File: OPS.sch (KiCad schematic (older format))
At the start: 92 parts, among them J1 USB, J2 PWR, J3 Banana, J4 Banana, J5 CON_PWR, J6 CON_DATA, J7 M3, P1 TC2030, Q1 SS8050, Q2 AO3400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

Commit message: routing 60%
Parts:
- C10, C15: value 100n -> 22u; footprint otter:C_0402 -> otter:C_0805
- C16, C20, C9: value 10u -> 22u
- C17, C8: footprint Capacitor_Tantalum_SMD:CP_EIA-7343-31_Kemet-D -> Capacitor_SMD:CP_Elec_6.3x5.8
- J6: footprint Connector_PinHeader_2.00mm:PinHeader_1x07_P2.00mm_Vertical -> Connector_PinHeader_2.00mm:PinHeader_1x08_P2.00mm_Vertical; symbol Connector_Generic:Conn_01x07 -> Connector_Generic:Conn_01x08
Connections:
- net +3V3: now also J6.4 (Pin_4)
- net INT_MP_1: now also J6.6 (Pin_6); no longer J6.5 (Pin_5)
- net LED_GREEN: now also U3.39 (PB3); no longer U3.40 (PB4)
- net LED_RED: now also U3.40 (PB4); no longer U3.39 (PB3)
- net OUT_EN_1: now also J6.5 (Pin_5); no longer J6.4 (Pin_4)
- net SCL: now also J6.7 (Pin_7); no longer J6.6 (Pin_6)
- net SDA: now also J6.8 (Pin_8); no longer J6.7 (Pin_7)
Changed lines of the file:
@@
 	7050 6300 7050 6400
 Connection ~ 7050 6300
-$Comp
-L Device:C_Small C10
-U 1 1 60808E89
-P 6700 6500
-F 0 "C10" H 6792 6546 50  0000 L CNN
-F 1 "100n" H 6792 6455 50  0000 L CNN
-F 2 "otter:C_0402" H 6700 6500 50  0001 C CNN
-F 3 "~" H 6700 6500 50  0001 C CNN
-	1    6700 6500
-	1    0    0    -1
-$EndComp
 Wire Wire Line
 	6700 6300 6700 6400
@@
 	6050 6250 6050 6300
 $Comp
-L otter:GND #PWR0137
-U 1 1 6082C1E8
-P 6700 6600
-F 0 "#PWR0137" H 6700 6350 50  0001 C CNN
-F 1 "GND" H 6705 6427 50  0000 C CNN
-F 2 "" H 6700 6600 60  0000 C CNN
-F 3 "" H 6700 6600 60  0000 C CNN
-	1    6700 6600
-	1    0    0    -1
-$EndComp
-$Comp
 L Device:C_Small C9
 U 1 1 60831902
 P 6400 6500
 F 0 "C9" H 6492 6546 50  0000 L CNN
-F 1 "10u" H 6492 6455 50  0000 L CNN
+F 1 "22u" H 6492 6455 50  0000 L CNN
 F 2 "otter:C_0805" H 6400 6500 50  0001 C CNN
 F 3 "~" H 6400 6500 50  0001 C CNN
@@
 F 0 "C8" H 6168 6496 50  0000 L CNN
 F 1 "47u" H 6168 6405 50  0000 L CNN
-F 2 "Capacitor_Tantalum_SMD:CP_EIA-7343-31_Kemet-D" H 6088 6300 50  0001 C CNN
+F 2 "Capacitor_SMD:CP_Elec_6.3x5.8" H 6088 6300 50  0001 C CNN
 F 3 "~" H 6050 6450 50  0001 C CNN
 	1    6050 6450
@@
 $EndComp
 $Comp
-L Device:C_Small C15
-U 1 1 6084818D
-P 8850 6900
-F 0 "C15" H 8942 6946 50  0000 L CNN
-F 1 "100n" H 8942 6855 50  0000 L CNN
-F 2 "otter:C_0402" H 8850 6900 50  0001 C CNN
-F 3 "~" H 8850 6900 50  0001 C CNN
-	1    8850 6900
-	1    0    0    -1
-$EndComp
-$Comp
-L otter:GND #PWR0140
-U 1 1 60848193
-P 8850 7000
-F 0 "#PWR0140" H 8850 6750 50  0001 C CNN
-F 1 "GND" H 8855 6827 50  0000 C CNN
-F 2 "" H 8850 7000 60  0000 C CNN
-F 3 "" H 8850 7000 60  0000 C CNN
-	1    8850 7000
-	1    0    0    -1
-$EndComp
-$Comp
 L Device:C_Small C16
 U 1 1 6084AEE7
 P 9200 6900
 F 0 "C16" H 9292 6946 50  0000 L CNN
-F 1 "10u" H 9292 6855 50  0000 L CNN
+F 1 "22u" H 9292 6855 50  0000 L CNN
 F 2 "otter:C_0805" H 9200 6900 50  0001 C CNN
 F 3 "~" H 9200 6900 50  0001 C CNN
@@
 F 0 "C17" H 9668 6946 50  0000 L CNN
 F 1 "47u" H 9668 6855 50  0000 L CNN
-F 2 "Capacitor_Tantalum_SMD:CP_EIA-7343-31_Kemet-D" H 9588 6750 50  0001 C CNN
+F 2 "Capacitor_SMD:CP_Elec_6.3x5.8" H 9588 6750 50  0001 C CNN
 F 3 "~" H 9550 6900 50  0001 C CNN
 	1    9550 6900
@@
 P 11800 6900
 F 0 "C20" H 11892 6946 50  0000 L CNN
-F 1 "10u" H 11892 6855 50  0000 L CNN
+F 1 "22u" H 11892 6855 50  0000 L CNN
 F 2 "otter:C_0805" H 11800 6900 50  0001 C CNN
 F 3 "~" H 11800 6900 50  0001 C CNN
@@
 Text GLabel 14250 7050 2    50   Input ~ 0
 LED_RED
+Text GLabel 8400 2800 0    50   Input ~ 0
+LED_GREEN
 Text GLabel 8400 2900 0    50   Input ~ 0
-LED_GREEN
-Text GLabel 8400 2800 0    50   Input ~ 0
 LED_RED
 Text Notes 13950 7350 0    50   ~ 0
@@
 	8050 3200 7800 3200
 Connection ~ 7800 3200
-Text GLabel 5650 5050 0    50   Input ~ 0
+Text GLabel 5650 5150 0    50   Input ~ 0
 INT_MP_1
-Text GLabel 5650 5150 0    50   Input ~ 0
+Text GLabel 5650 5250 0    50   Input ~ 0
 SCL
-Text GLabel 5650 5250 0    50   Input ~ 0
+Text GLabel 5650 5350 0    50   Input ~ 0
 SDA
 $Comp
-L Connector_Generic:Conn_01x07 J6
+L Connector_Generic:Conn_01x08 J6
 U 1 1 60960B7E
 P 5850 4950
 F 0 "J6" H 5930 4992 50  0000 L CNN
 F 1 "CON_DATA" H 5930 4901 50  0000 L CNN
-F 2 "Connector_PinHeader_2.00mm:PinHeader_1x07_P2.00mm_Vertical" H 5850 4950 50  0001 C CNN
+F 2 "Connector_PinHeader_2.00mm:PinHeader_1x08_P2.00mm_Vertical" H 5850 4950 50  0001 C CNN
 F 3 "~" H 5850 4950 50  0001 C CNN
 	1    5850 4950
@@
 Text GLabel 11350 3400 2    50   Input ~ 0
 OUT_EN_1
-Text GLabel 5650 4950 0    50   Input ~ 0
+Text GLabel 5650 5050 0    50   Input ~ 0
 OUT_EN_1
 $Comp
@@
 Wire Wire Line
 	10200 3200 9700 3200
+$Comp
+L Device:C_Small C10
+U 1 1 60860E99
+P 6700 6500
+F 0 "C10" H 6792 6546 50  0000 L CNN
+F 1 "22u" H 6792 6455 50  0000 L CNN
+F 2 "otter:C_0805" H 6700 6500 50  0001 C CNN
+F 3 "~" H 6700 6500 50  0001 C CNN
+	1    6700 6500
+	1    0    0    -1
+$EndComp
+$Comp
+L otter:GND #PWR0137
+U 1 1 60860E9F
+P 6700 6600
+F 0 "#PWR0137" H 6700 6350 50  0001 C CNN
+F 1 "GND" H 6705 6427 50  0000 C CNN
+F 2 "" H 6700 6600 60  0000 C CNN
+F 3 "" H 6700 6600 60  0000 C CNN
+	1    6700 6600
+	1    0    0    -1
+$EndComp
+$Comp
+L Device:C_Small C15
+U 1 1 60872DD9
+P 8850 6900
+F 0 "C15" H 8942 6946 50  0000 L CNN
+F 1 "22u" H 8942 6855 50  0000 L CNN
+F 2 "otter:C_0805" H 8850 6900 50  0001 C CNN
+F 3 "~" H 8850 6900 50  0001 C CNN
+	1    8850 6900
+	1    0    0    -1
+$EndComp
+$Comp
+L otter:GND #PWR0140
+U 1 1 60872DDF
+P 8850 7000
+F 0 "#PWR0140" H 8850 6750 50  0001 C CNN
+F 1 "GND" H 8855 6827 50  0000 C CNN
+F 2 "" H 8850 7000 60  0000 C CNN
+F 3 "" H 8850 7000 60  0000 C CNN
+	1    8850 7000
+	1    0    0    -1
+$EndComp
+$Comp
+L power:+3V3 #PWR0185
+U 1 1 6092E1C5
+P 5650 4950
+F 0 "#PWR0185" H 5650 4800 50  0001 C CNN
+F 1 "+3V3" V 5665 5078 50  0000 L CNN
+F 2 "" H 5650 4950 50  0001 C CNN
+F 3 "" H 5650 4950 50  0001 C CNN
+	1    5650 4950
+	0    -1   -1   0
+$EndComp
 $EndSCHEMATC

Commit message: routing 99%
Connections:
- net +3V3: now also SW1.1; no longer SW1.2
- net at R5.1, U3.44 (BOOT0): now also SW1.2; no longer SW1.1
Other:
- moved on the sheet: SW1
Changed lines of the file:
@@
 F 3 "~" H 7750 1550 50  0001 C CNN
 	1    7750 1350
-	0    -1   -1   0
+	0    1    1    0
 $EndComp
 Wire Wire Line

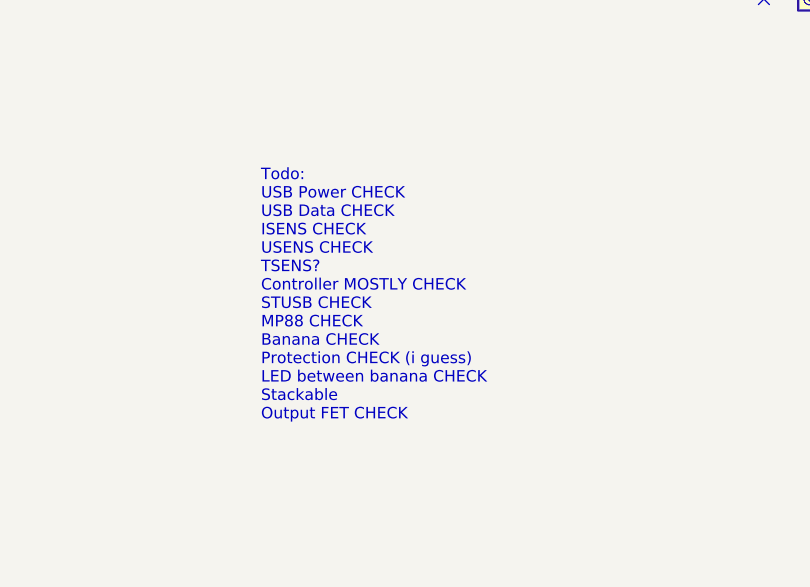
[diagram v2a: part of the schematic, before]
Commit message: updated silk
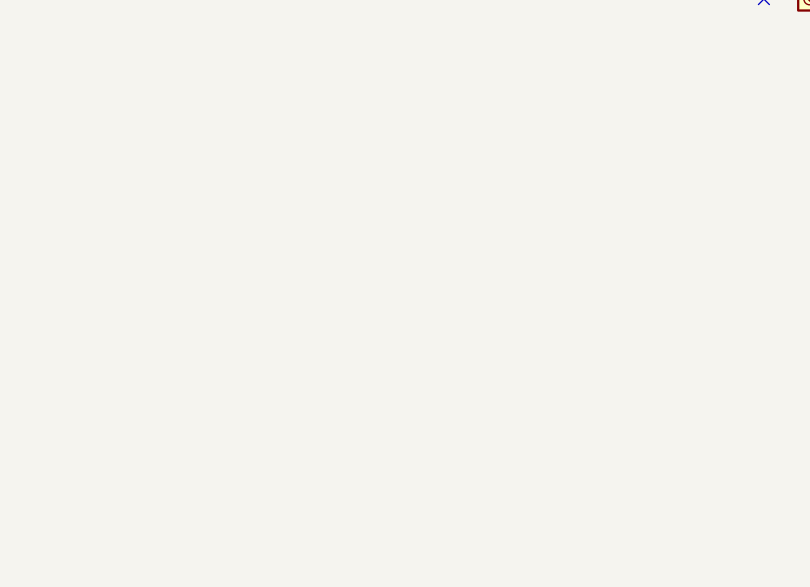
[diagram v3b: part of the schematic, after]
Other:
- note removed: "Todo:\nUSB Power CHECK\nUSB Data CHECK\nISENS CHECK\nUSENS CHECK\nTSENS?\nController MOSTLY CHECK\nSTUSB CHECK\nMP88 CHECK\nBanana CHECK\nProtection CHECK (i guess)\nLED between banana CHECK\nStackable\nOutput FET CHECK"
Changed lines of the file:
@@
 	0    -1   -1   0
 $EndComp
-Text Notes 3150 7450 0    50   ~ 0
-Todo:\nUSB Power CHECK\nUSB Data CHECK\nISENS CHECK\nUSENS CHECK\nTSENS?\nController MOSTLY CHECK\nSTUSB CHECK\nMP88 CHECK\nBanana CHECK\nProtection CHECK (i guess)\nLED between banana CHECK\nStackable\nOutput FET CHECK
 $Comp
 L otter:GND #PWR0101
